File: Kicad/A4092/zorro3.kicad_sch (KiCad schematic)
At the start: 13 parts, among them CN1 Zorro3, U1 SN74ABT16543DGGR, U2 SN74ABT16543DGGR, U3 SN74ABT16543DGGR, U4 SN74ABT16543DGGR, U5 74LVC07APW_118, U6 SN74ABT16245ADGGR

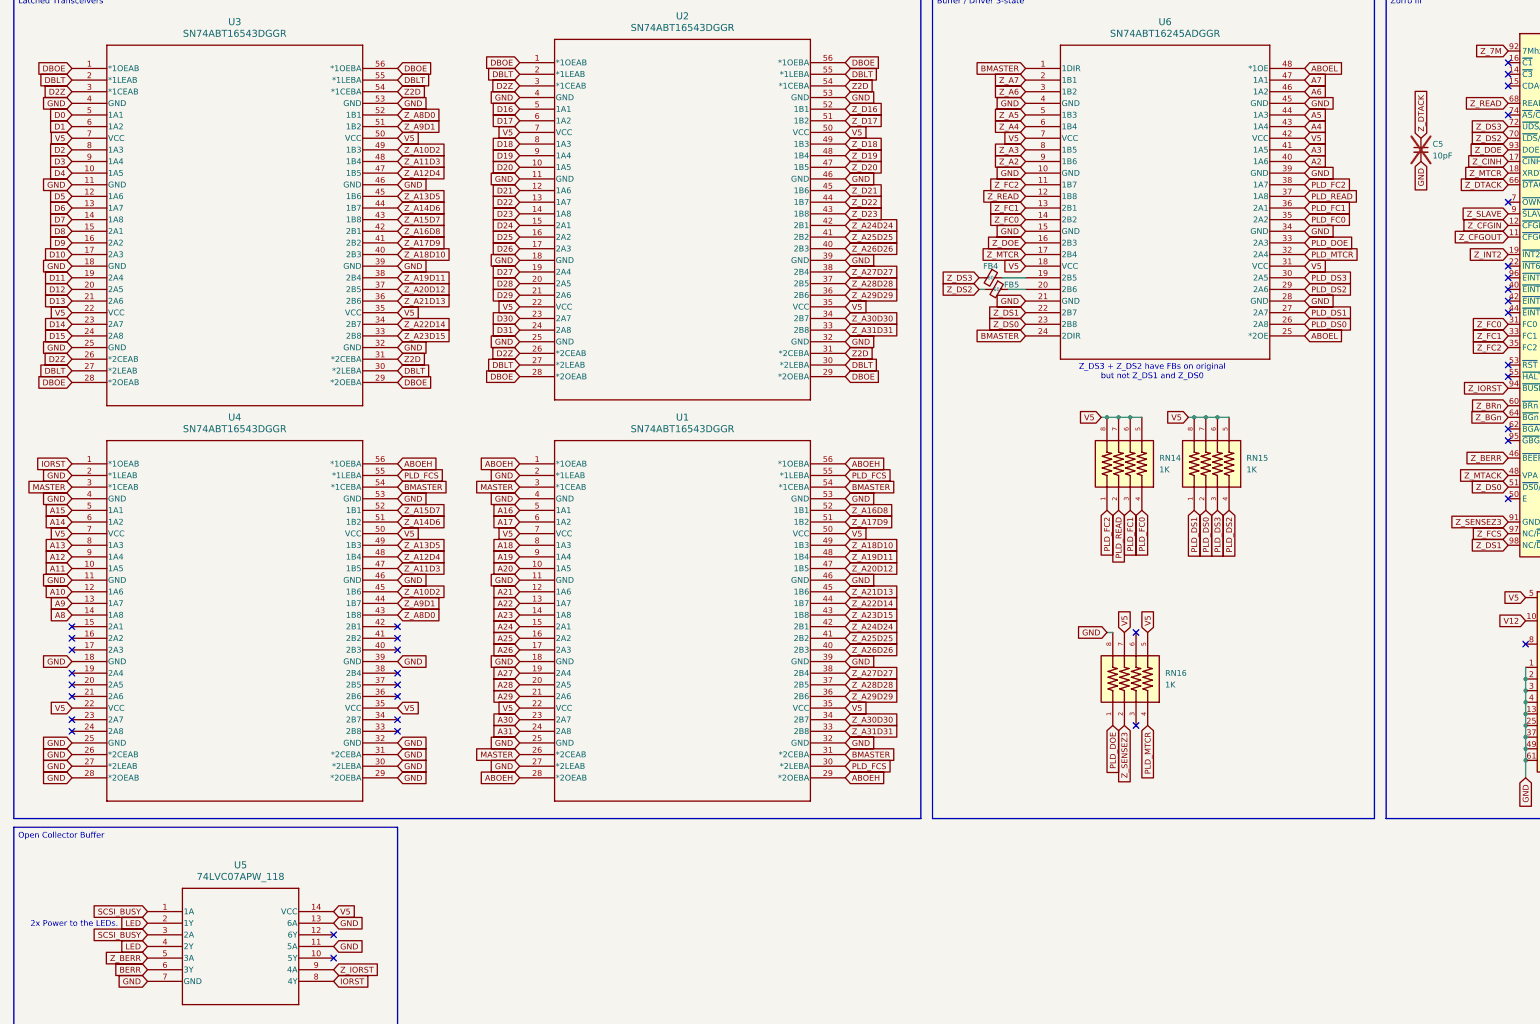
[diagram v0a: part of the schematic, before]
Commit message: A4092 Schematics Revision C
- Power U5 / 74LVC07 from 3.3V rail
- Use ABOEH for 1OEAB on U4 / 74ABT16543
- Add bypass capacitor C501 for U5 / 74LVC07
- Remove EMI filters and capacitors from SCSI lines. They
  are a net negative for signal integrity
- Remove DIP switch circuit as all options are controlled
  by the CPLD / AutoConfig ROM now.
- Remove parallel flash memory, as SPI works reliably and
  is significantly easier to source.
- Remove all ferrite beads from signal lines, as these were
  populated with 0 Ohm resistors in all Proto devices.
- Mark power connector and 12V capacitor as DNP
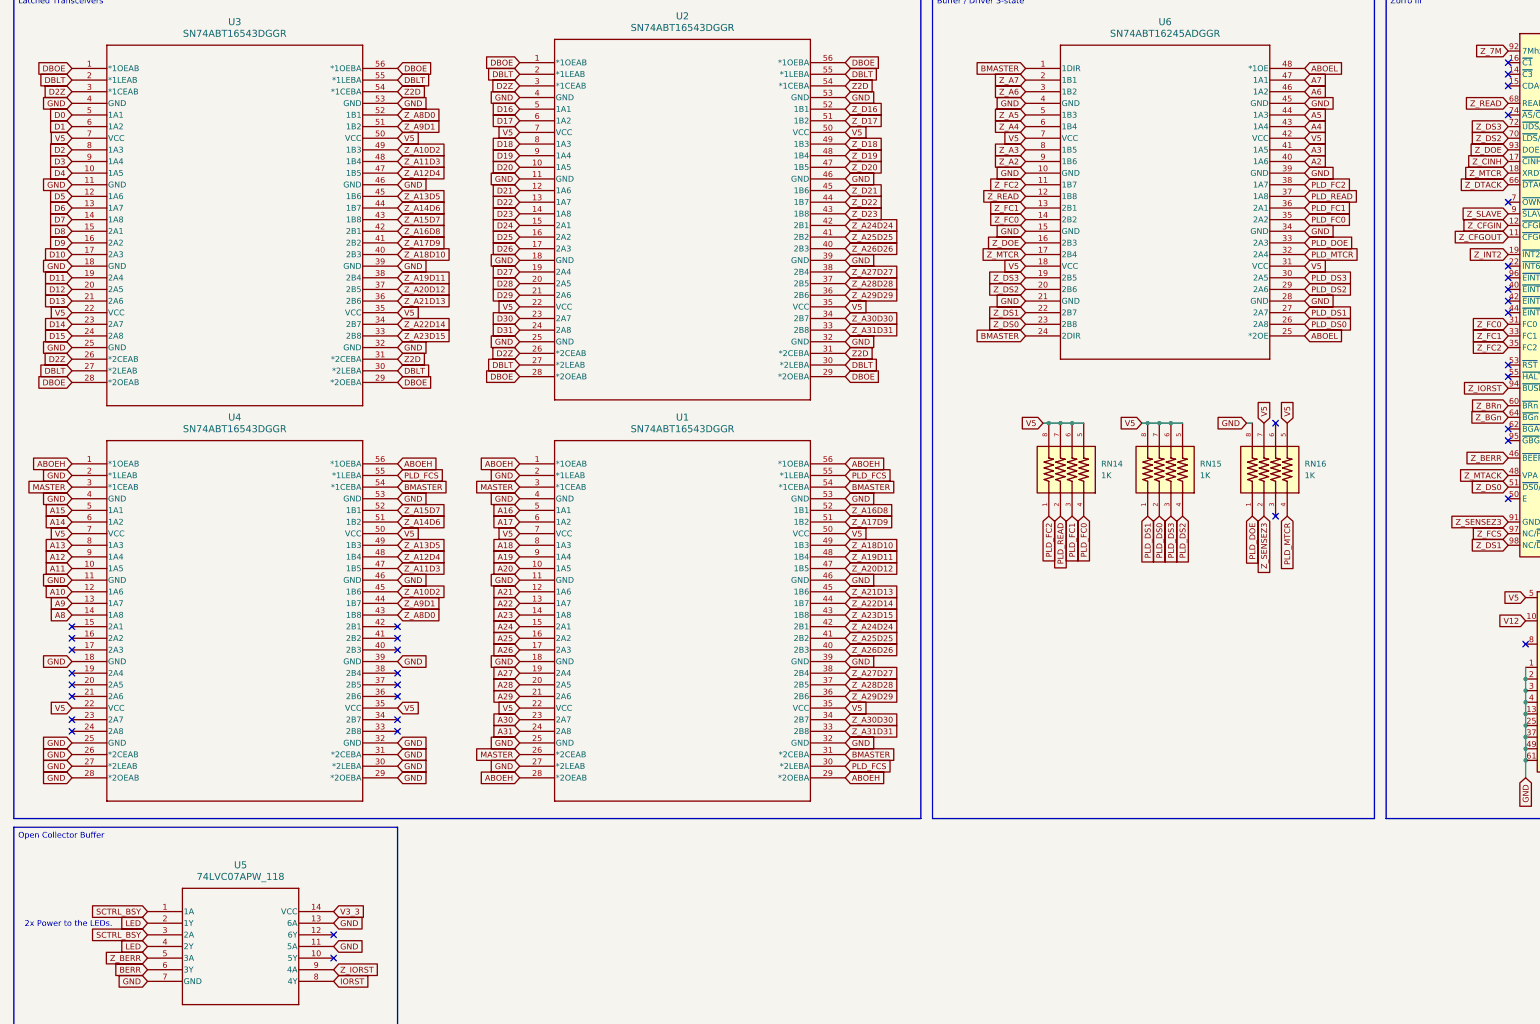
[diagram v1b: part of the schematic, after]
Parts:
- removed C5: 10pF, Capacitor_SMD:C_0603_1608Metric_Pad1.08x0.95mm_HandSolder, symbol Device:C_Small
- removed FB4, FB5: 60, Capacitor_SMD:C_0603_1608Metric_Pad1.08x0.95mm_HandSolder, symbol Device:FerriteBead_Small
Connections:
- net ABOEH: now also U4.1 (*1OEAB)
- net IORST: no longer U4.1 (*1OEAB)
- net V5: no longer U5.14 (VCC)
- net Z_DS2: now also U6.20 (2B6)
- net Z_DS3: now also U6.19 (2B5)
- net SCSI_BUSY renamed SCTRL_BSY
- new net V3_3: U5.14 (VCC)
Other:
- note removed: "Z_DS3 + Z_DS2 have FBs on original but not Z_DS1 and Z_DS0"
- moved on the sheet: RN14, RN15, RN16

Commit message: Fix footprint references in schematics
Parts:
- U1, U2, U3, U4: footprint DGG56 -> SN74ABT16543DGGR:DGG56
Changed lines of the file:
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@@
 			)
 		)
-		(property "Footprint" "DGG56"
+		(property "Footprint" "SN74ABT16543DGGR:DGG56"
 			(at 125.73 118.11 0)
 			(effects
@@
 			)
 		)
-		(property "Footprint" "DGG56"
+		(property "Footprint" "SN74ABT16543DGGR:DGG56"
 			(at 27.94 31.75 0)
 			(effects
@@
 			)
 		)
-		(property "Footprint" "DGG56"
+		(property "Footprint" "SN74ABT16543DGGR:DGG56"
 			(at 27.94 118.11 0)
 			(effects
@@
 			)
 		)
-		(property "Footprint" "DGG56"
+		(property "Footprint" "SN74ABT16543DGGR:DGG56"
 			(at 125.73 30.48 0)
 			(effects
